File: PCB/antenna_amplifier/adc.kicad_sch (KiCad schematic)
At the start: 34 parts, among them SW301 RESET, SW302 PCM1804 MODE, U301 LMP7715, U302 PCM1804

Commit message: Add two-bucket isolated PSU and the PC analysis software
PSU (PCB/acdc_converter/design.py, generated schematic, ERC clean):
Mains -> IRM-05-15 -> LM317 constant-current (0.2 A) / constant-voltage
(10.9 V) supercap charger -> two 4 x 10 F buckets swapped every ~30 s by
two Omron G6K-2 DPDT relays wired in opposite senses. Form-C contacts
break before make, so the receiver ground is never connected to the
charger side; the only coupling left is the open-contact capacitance
(~1 pF) instead of the AC-DC barrier (20-100 pF). The receiver side
adds a reservoir, an LT3045 (0.8 uV rms, EN/PGFB to IN, 22 uF C_SET for
low 1/f noise) and a common-mode choke. Charger ground is bonded to PE
and the enclosure; the only LED is on the mains-powered charger side.

Software (software/elara): streaming decimator, PLL-locked NLMS mains
canceller (>60 dB with drift, 45 Hz tone untouched), L/R Wiener noise
reference subtraction, front-end response correction, Lorentzian
Schumann fit, sferic detector, simulator and CLI; 27 pytest tests.

Generator: explicit wires, net labels on wires, touching and stacked
pins, labels-only symbols.

Co-Authored-By: Claude Opus 5.5 <noreply@anthropic.com>
Claude-Session: https://claude.ai/code/session_01RsM1DhHhY1tSr2aHjVygSC
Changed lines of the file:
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@@
 		(dnp no)
 		(property "Reference" "SW301"
-			(at 395.01 100.6 270)
+			(at 395.01 100.6 90)
 			(effects
 				(font
@@
 		)
 		(property "Value" "RESET"
-			(at 395.01 103.2 270)
+			(at 395.01 103.2 90)
 			(effects
 				(font

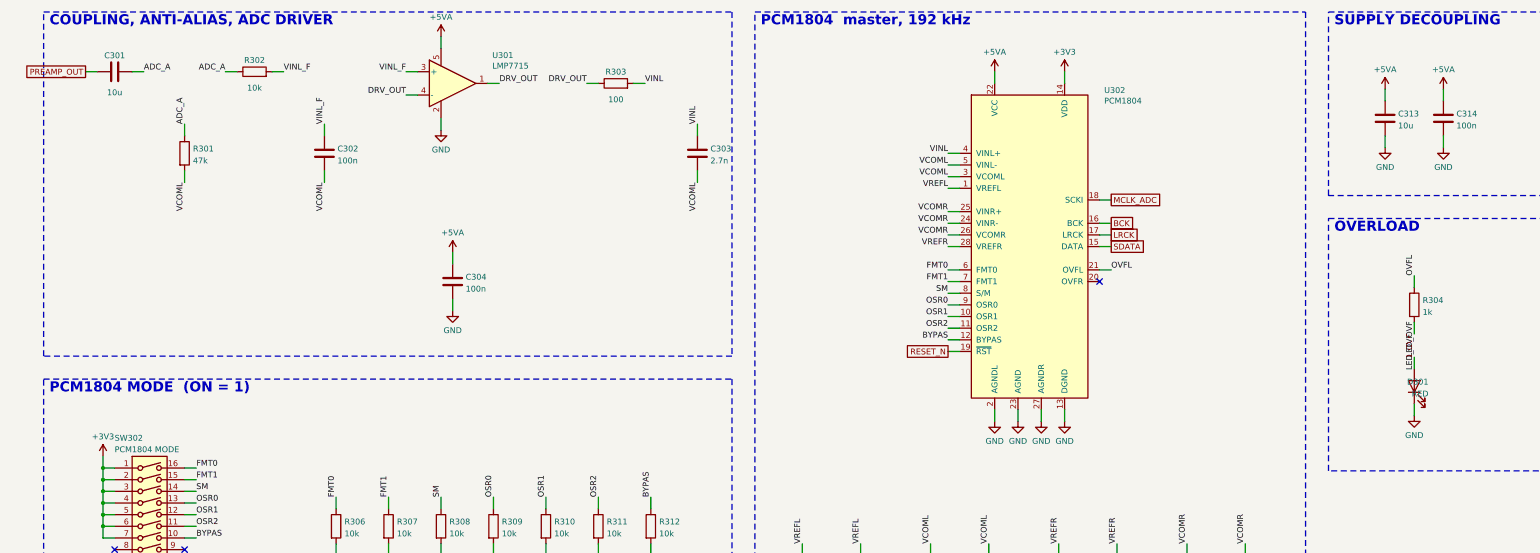
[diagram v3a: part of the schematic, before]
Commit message: Pedantic schematic and silkscreen pass: zero overlaps, labels clear of tracks
Schematics
- tools/kicadgen/schcheck.py checks KiCad's own SVG rendering (exact stroke boxes)
  for text over text, lines through text, crowded twin labels and text outside the
  frame. Both schematics: 0 findings; ERC 0 on both.
- Generator: Sheet.join (one wire + one label instead of two facing labels),
  per-symbol field positions, per-pin stub lengths, shared power symbol for
  adjacent top/bottom rail pins, crowded rail runs get one label, longer PCM1804
  pins (no-connect cross clear of the pin number), PE value clear of its symbol.
- Fixed: doubled VIN_RAW/BIAS_DIV/LED_OVF/CV_ADJ/LED_C labels, +5VA vs VREG,
  +5V_PRE twins, CS8406 GND straps vs neighbours, BNC/LED/diode fields over their
  graphics, bucket-cell values vs tap labels, notes outside the frame, J2 -> J202.
- Root sheet: sub-sheets in signal-flow order with arrows and a design summary;
  dated title blocks.

Boards
- References prefer spots clear of tracks as well as parts (two candidate rings);
  compartment labels are re-placed after routing; the title block on the back is
  placed as one unit; no stitching via under any board text.
- DRC with schematic parity: amplifier 0 errors / 0 unconnected / 0 parity (only
  the intended bare-island mask warnings); PSU and plate 0 of anything.

Co-Authored-By: Claude Opus 5.5 <noreply@anthropic.com>
Claude-Session: https://claude.ai/code/session_01RsM1DhHhY1tSr2aHjVygSC
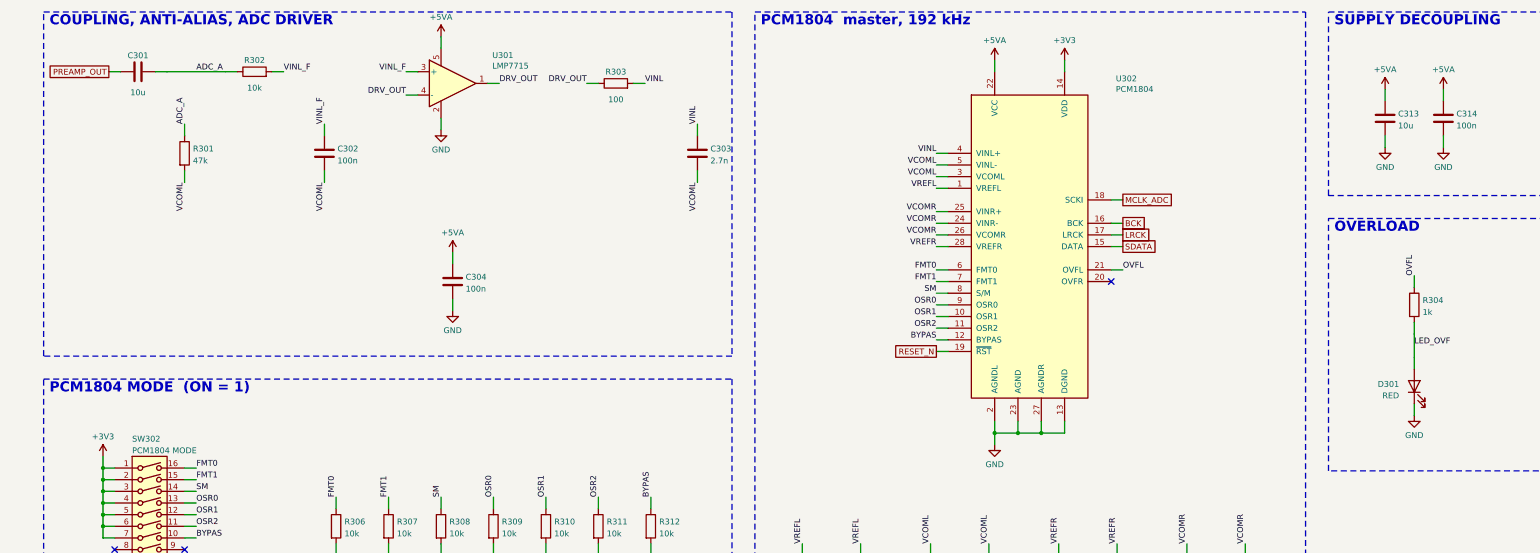
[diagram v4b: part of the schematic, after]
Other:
- moved on the sheet: C301

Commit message: Amplifier: single BNC, pluggable AES3, real 63 V Cg, wall clearances
From the placement and parts audit:
- J402 was an Amphenol 031-6575, a dual stacked BNC 29 mm tall that
  could never pass the 14 mm wall notch. Now a single right-angle
  B6252HB-NPP3G-50 (KiCad model), body inside the compartment and
  only the nut/barrel through the notch.
- J401's screw terminals sat under the right wall (screws at x = 194,
  wall from 193) and the shield mounts lid-down, so the AES3 cable could
  not be wired in place. Now a Phoenix MC 1,5/3-G-3,81 right-angle
  header: the MC 1,5/3-ST-3,81 plug is wired outside and pushed in
  through the notch (16 x 13 mm).
- C202's order code was the 100 VDC WIMA (24 x 45.5 mm) on a 35 mm
  footprint. Now MKS4C061007G00KSSD (63 VDC, 41.5 x 20 x 39.5 mm) on the
  matching footprint; C301 on its real 8.5 mm footprint.
- J101 moved 1.5 mm so its body is centred in its notch (was 0.6 mm
  from the notch side); C101, C205 and TR402 moved off the walls.
- ANT_BIAS leaves the island stub through a via so it can reach In2.
- Fab-layer values hidden on both boards: the assembly drawing now shows
  clean references (values are in the BOMs). The STEP export uses the
  board corner as origin for the mechanical fit checks.
DRC: amplifier 77 intended island mask bridges only, PSU 0; unconnected
0 and parity 0 on both; ERC 0; schematic legibility 0.

Co-Authored-By: Claude Opus 5.5 <noreply@anthropic.com>
Claude-Session: https://claude.ai/code/session_01RsM1DhHhY1tSr2aHjVygSC
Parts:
- C301: footprint Capacitor_THT:C_Rect_L26.5mm_W11.5mm_P22.50mm_MKS4 -> Capacitor_THT:C_Rect_L26.5mm_W8.5mm_P22.50mm_MKS4; MPN MKS4 10uF 63V PCM22.5 -> MKS4C051005F00KSSD
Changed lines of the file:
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@@
 			)
 		)
-		(property "Footprint" "Capacitor_THT:C_Rect_L26.5mm_W11.5mm_P22.50mm_MKS4"
+		(property "Footprint" "Capacitor_THT:C_Rect_L26.5mm_W8.5mm_P22.50mm_MKS4"
 			(at 35.56 33.02 0)
 			(effects
@@
 			)
 		)
-		(property "Description" "Film 10u 63V PET, PCM 22.5 mm (C_out)"
+		(property "Description" "Film 10u 63 VDC PET, PCM 22.5 mm, 26.5 x 8.5 x 18.5 mm (C_out)"
 			(at 35.56 33.02 0)
 			(effects
@@
 			)
 		)
-		(property "MPN" "MKS4 10uF 63V PCM22.5"
+		(property "MPN" "MKS4C051005F00KSSD"
 			(at 35.56 33.02 0)
 			(effects

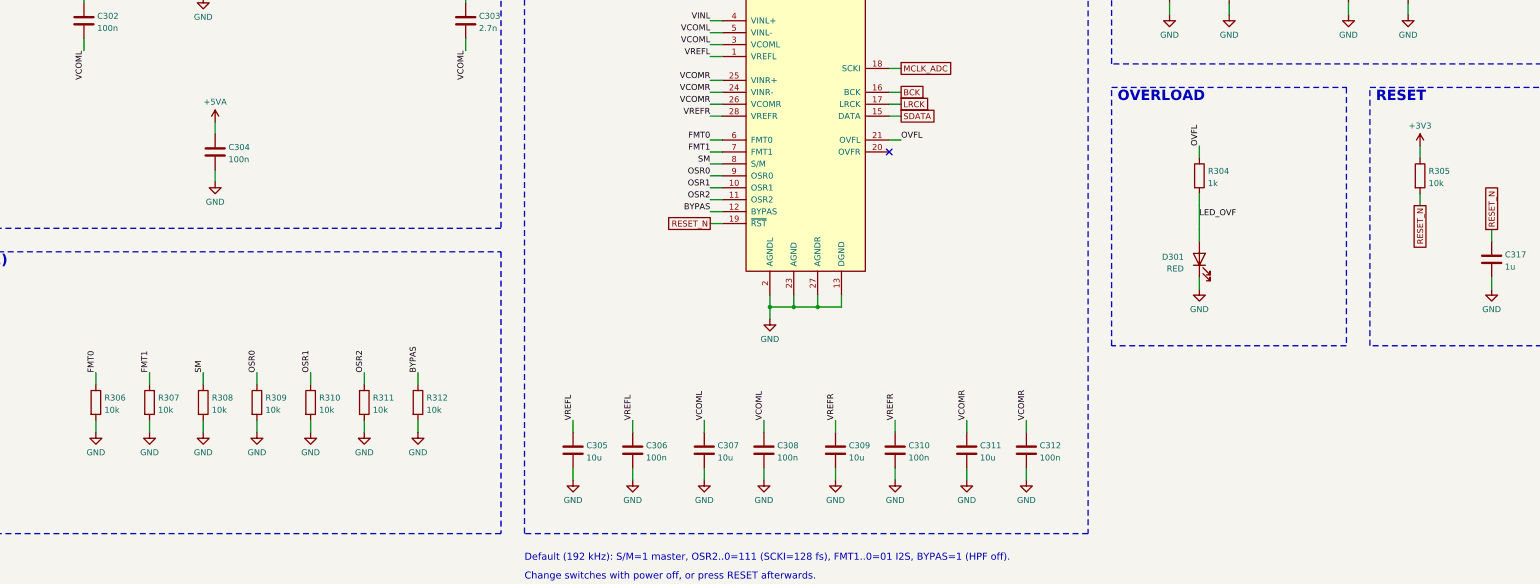
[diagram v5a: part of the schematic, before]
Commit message: Battery-friendly amplifier, RJ45 AES3 output, tidy placement, 1 mm PSU barrier
Amplifier schematic:
- No LEDs (battery use): the D301 overflow LED becomes test point TP301.
- PCM1804 FMT/S-M/OSR pins use the chip's internal 51 k pull-downs (6 resistors
  gone); BYPAS and the CS8406 mode pins get 47 k: about 3 mA less on +3V3.
- One output: AES3 on a shielded RJ45 (Amphenol RJHSE-5380, blue pair 4/5) for
  shielded twisted-pair cable, transformer isolated; the cable shield floats at
  the receiver (10 nF RF bond DNP, the DC bond is gone). The S/PDIF coax branch
  (BNC, second S22083, 5.6 mA standing current) is removed.

Layout:
- Amplifier re-placed in functional blocks on a 0.5 mm grid: PCM1804 and CS8406
  side by side so the I2S lines run straight, capacitor cells round the LDOs,
  DIP pull-downs in line with the switch pins, guard column in signal order with
  a re-routed hand guard-drive link. RJ45 notch 20 x 16 mm, BNC notch gone.
- PSU tidied (aligned columns, flyback diodes over their relays) and the charger
  / receiver copper kept >= 1.0 mm apart (was 0.30 mm): custom DRC rule, 1 mm
  router class for the relay contacts, hand-routed GND / GND_C at the relays.
- Reference labels follow each part's row; every label on silk except on the
  bare guard island. Fixed two placer bugs: each label counted as its own
  obstacle (SWIG proxies compared with 'is'), and unplaced labels blocked their
  neighbours. Texts are measured by their strokes, not KiCad's text cell.

Mechanics: RJ45 notch, plug envelope and a 1 mm isolation gap in fit_check.
BOM: 502 EUR as designed, 407 EUR recommended; 81 order lines.
Docs: STATUS, PLAN, ASSEMBLY, MOUNTING, README, mechanical and BOM notes;
MAINS_CABLE gains a certified DIY screened-cable option (H07RN-F + foil + braid)
and says why Ethernet cable must not carry mains.

All checks pass (tools/check_all.sh): ERC 0, DRC/parity 0 on all boards (only
the intended guard-island mask bridges), mains clearances, fit check, 27 tests.

Co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
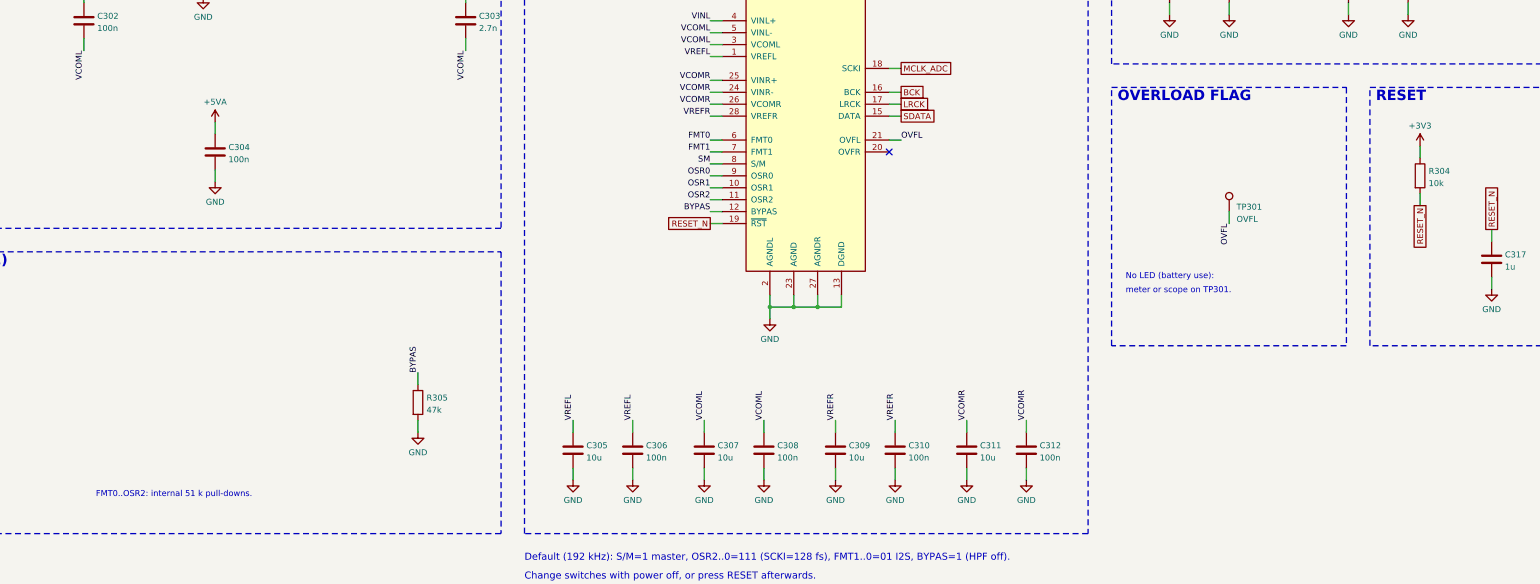
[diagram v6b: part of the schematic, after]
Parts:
- removed D301: RED, LED_SMD:LED_0805_2012Metric, symbol Device:LED
- removed R306, R307, R308, R309, R310, R311, R312: 10k, Resistor_SMD:R_0603_1608Metric, symbol Device:R
- added TP301: OVFL, TestPoint:TestPoint_Keystone_5000-5004_Miniature, symbol Connector:TestPoint
- R304: value 1k -> 10k; MPN ERA-3AEB102V -> ERA-3AEB103V
- R305: value 10k -> 47k; MPN ERA-3AEB103V -> ERA-3AEB473V; Role (none) -> pull-down (no internal one on BYPAS)
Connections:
- net LED_OVF is gone; now on net RESET_N: R304.2
- net +3V3: now also R304.1; no longer R305.1
- net BYPAS: now also R305.1
- net GND: now also R305.2
- net OVFL: now also TP301.1; no longer R304.1
- net RESET_N: no longer R305.2
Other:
- note added: "FMT0..OSR2: internal 51 k pull-downs."
- note added: "No LED (battery use):"
- note added: "OVERLOAD FLAG"
- note added: "meter or scope on TP301."
- note removed: "OVERLOAD"
- moved on the sheet: R304, R305
